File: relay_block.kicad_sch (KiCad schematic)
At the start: 49 parts, among them J4 Screw_Terminal_01x02, J5 Screw_Terminal_01x10, J6 Screw_Terminal_01x10, U10 TLP3558A, U11 TLP3558A, U12 TLP3558A, U13 TLP3558A, U14 TLP3558A, U15 TLP3558A, U16 TLP3558A, U17 TLP3558A, U18 TLP3558A, U19 TLP3558A, U20 TLP3558A, U21 TLP3558A, U22 TLP3558A, U23 TLP3558A, U24 TLP3558A, U25 TLP3558A, U4 TLP3558A, U5 TLP3558A, U6 TLP3558A, U7 TLP3558A, U8 TLP3558A, U9 TLP3558A

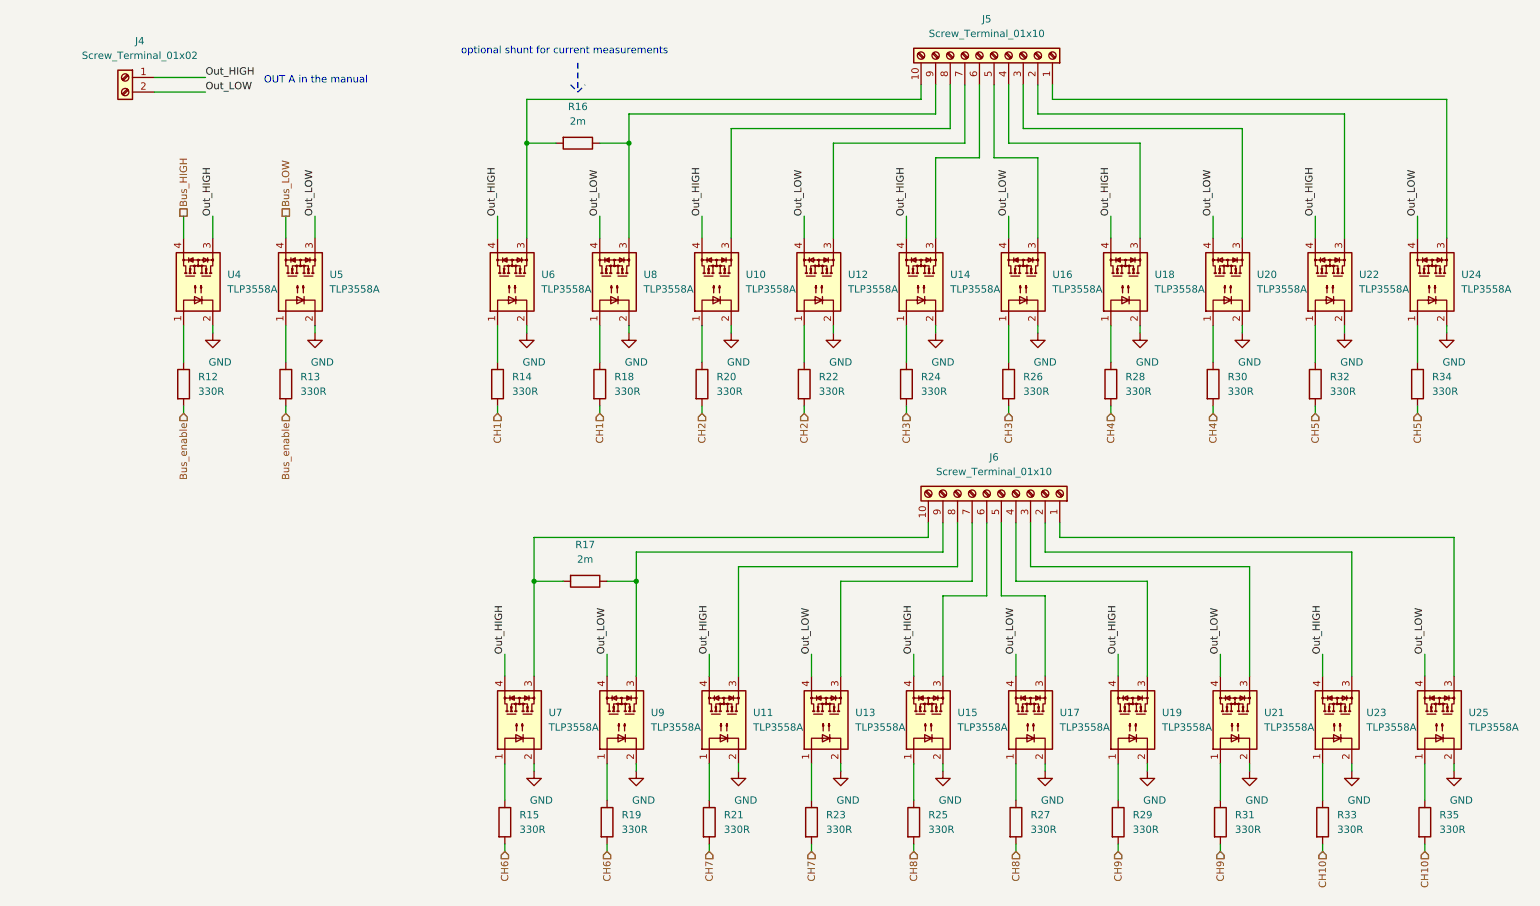
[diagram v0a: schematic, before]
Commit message: Replace the STM32 with an iCE40 FPGA (#3)
* Replaced the STM32 microcontroller with an iCE40 FPGA

* Bump version to 2.0.2, because of the update to KiCad 8

* Updated BOM properties

* Updated PCB image

* Updated readme for the FPGA version

* Updated links
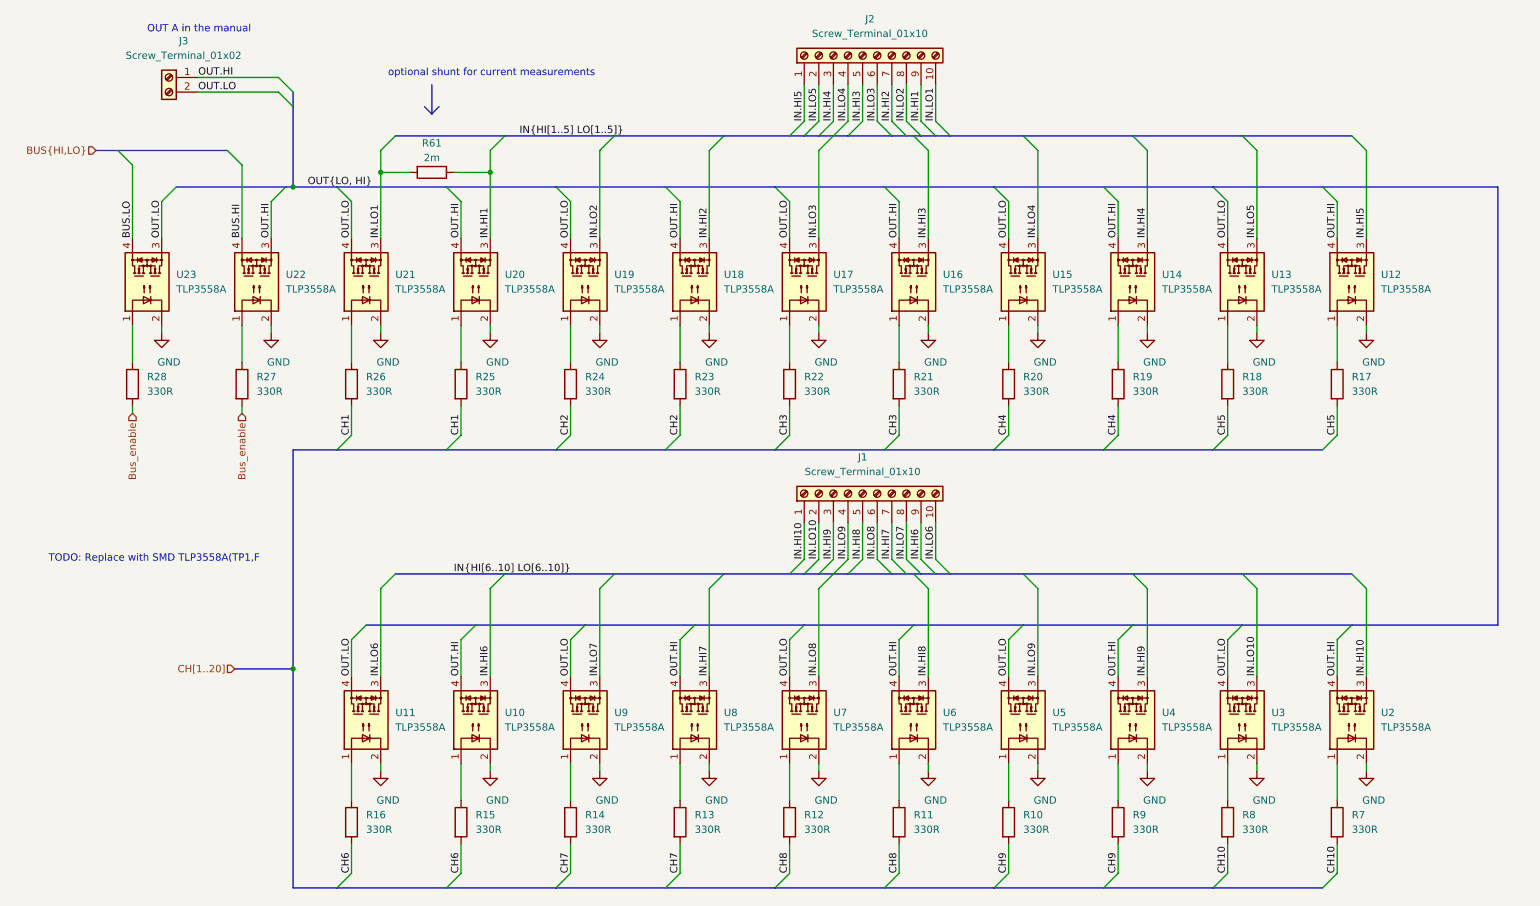
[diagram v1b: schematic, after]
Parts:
- removed R17: 2m, Resistor_SMD:R_2512_6332Metric, symbol Device:R
- J1: renamed from J6; RoHS By exemption -> Yes; Temperature Tstorage = –40 °C to 105 °C -> (none)
- J2: renamed from J5; RoHS By exemption -> Yes; Temperature Tstorage = –40 °C to 105 °C -> (none)
- J3: renamed from J4; RoHS By exemption -> Yes; Temperature Tstorage = –40 °C to 105 °C -> (none)
- R10: renamed from R29; Alternative (none) -> Yageo AC0603JR-07330RL or AC0603FR-07330RL; Note (none) -> 5% or better; PN CRCW0603330RJNEB -> CRCW0603330RJNEA
- R11: renamed from R27; Alternative (none) -> Yageo AC0603JR-07330RL or AC0603FR-07330RL; Note (none) -> 5% or better; PN CRCW0603330RJNEB -> CRCW0603330RJNEA
- R12: renamed from R25; Alternative (none) -> Yageo AC0603JR-07330RL or AC0603FR-07330RL; Note (none) -> 5% or better; PN CRCW0603330RJNEB -> CRCW0603330RJNEA
- R13: renamed from R23; Alternative (none) -> Yageo AC0603JR-07330RL or AC0603FR-07330RL; Note (none) -> 5% or better; PN CRCW0603330RJNEB -> CRCW0603330RJNEA
- R14: renamed from R21; Alternative (none) -> Yageo AC0603JR-07330RL or AC0603FR-07330RL; Note (none) -> 5% or better; PN CRCW0603330RJNEB -> CRCW0603330RJNEA
- R15: renamed from R19; Alternative (none) -> Yageo AC0603JR-07330RL or AC0603FR-07330RL; Note (none) -> 5% or better; PN CRCW0603330RJNEB -> CRCW0603330RJNEA
- R16: renamed from R15; Alternative (none) -> Yageo AC0603JR-07330RL or AC0603FR-07330RL; Note (none) -> 5% or better; PN CRCW0603330RJNEB -> CRCW0603330RJNEA
- R17: renamed from R34; Alternative (none) -> Yageo AC0603JR-07330RL or AC0603FR-07330RL; Note (none) -> 5% or better; PN CRCW0603330RJNEB -> CRCW0603330RJNEA
- R18: renamed from R32; Alternative (none) -> Yageo AC0603JR-07330RL or AC0603FR-07330RL; Note (none) -> 5% or better; PN CRCW0603330RJNEB -> CRCW0603330RJNEA
- R19: renamed from R30; Alternative (none) -> Yageo AC0603JR-07330RL or AC0603FR-07330RL; Note (none) -> 5% or better; PN CRCW0603330RJNEB -> CRCW0603330RJNEA
- R20: renamed from R28; Alternative (none) -> Yageo AC0603JR-07330RL or AC0603FR-07330RL; Note (none) -> 5% or better; PN CRCW0603330RJNEB -> CRCW0603330RJNEA
- R21: renamed from R26; Alternative (none) -> Yageo AC0603JR-07330RL or AC0603FR-07330RL; Note (none) -> 5% or better; PN CRCW0603330RJNEB -> CRCW0603330RJNEA
- R22: renamed from R24; Alternative (none) -> Yageo AC0603JR-07330RL or AC0603FR-07330RL; Note (none) -> 5% or better; PN CRCW0603330RJNEB -> CRCW0603330RJNEA
- R23: renamed from R22; Alternative (none) -> Yageo AC0603JR-07330RL or AC0603FR-07330RL; Note (none) -> 5% or better; PN CRCW0603330RJNEB -> CRCW0603330RJNEA
- R24: renamed from R20; Alternative (none) -> Yageo AC0603JR-07330RL or AC0603FR-07330RL; Note (none) -> 5% or better; PN CRCW0603330RJNEB -> CRCW0603330RJNEA
- R25: renamed from R18; Alternative (none) -> Yageo AC0603JR-07330RL or AC0603FR-07330RL; Note (none) -> 5% or better; PN CRCW0603330RJNEB -> CRCW0603330RJNEA
- R26: renamed from R14; Alternative (none) -> Yageo AC0603JR-07330RL or AC0603FR-07330RL; Note (none) -> 5% or better; PN CRCW0603330RJNEB -> CRCW0603330RJNEA
- R27: renamed from R12; Alternative (none) -> Yageo AC0603JR-07330RL or AC0603FR-07330RL; Note (none) -> 5% or better; PN CRCW0603330RJNEB -> CRCW0603330RJNEA
- R28: renamed from R13; Alternative (none) -> Yageo AC0603JR-07330RL or AC0603FR-07330RL; Note (none) -> 5% or better; PN CRCW0603330RJNEB -> CRCW0603330RJNEA
- R61: renamed from R16; Config (none) -> do not fit
- R7: renamed from R35; Alternative (none) -> Yageo AC0603JR-07330RL or AC0603FR-07330RL; Note (none) -> 5% or better; PN CRCW0603330RJNEB -> CRCW0603330RJNEA
- R8: renamed from R33; Alternative (none) -> Yageo AC0603JR-07330RL or AC0603FR-07330RL; Note (none) -> 5% or better; PN CRCW0603330RJNEB -> CRCW0603330RJNEA
- R9: renamed from R31; Alternative (none) -> Yageo AC0603JR-07330RL or AC0603FR-07330RL; Note (none) -> 5% or better; PN CRCW0603330RJNEB -> CRCW0603330RJNEA
- renumbered U9 to U10, U7 to U11, U24 to U12, U22 to U13, U20 to U14, U18 to U15, U14 to U17, U12 to U18, U10 to U19, U25 to U2, U8 to U20, U6 to U21, U4 to U22, U5 to U23, U23 to U3, U21 to U4, U19 to U5, U17 to U6, U15 to U7, U13 to U8, U11 to U9
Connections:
- net IN.LO1: now reaches J2.10 (Pin_10), R61.2, U21.3
- net IN.HI1: now reaches J2.9 (Pin_9), R61.1, U20.3
- net IN.HI5: now reaches J2.1 (Pin_1), U12.3
- net IN.LO5: now reaches J2.2 (Pin_2), U13.3
- net IN.HI4: now reaches J2.3 (Pin_3), U14.3
- net IN.LO4: now reaches J2.4 (Pin_4), U15.3
- net IN.HI3: now reaches J2.5 (Pin_5), U16.3
- net IN.LO3: now reaches J2.6 (Pin_6), U17.3
- net IN.HI2: now reaches J2.7 (Pin_7), U18.3
- net IN.LO2: now reaches J2.8 (Pin_8), U19.3
- net IN.LO6: now reaches J1.10 (Pin_10), U11.3
- net IN.HI10: now reaches J1.1 (Pin_1), U2.3
- net IN.LO10: now reaches J1.2 (Pin_2), U3.3
- net IN.HI9: now reaches J1.3 (Pin_3), U4.3
- net IN.LO9: now reaches J1.4 (Pin_4), U5.3
- net IN.HI8: now reaches J1.5 (Pin_5), U6.3
- net IN.LO8: now reaches J1.6 (Pin_6), U7.3
- net IN.HI7: now reaches J1.7 (Pin_7), U8.3
- net IN.LO7: now reaches J1.8 (Pin_8), U9.3
- net IN.HI6: now reaches J1.9 (Pin_9), U10.3
- net Bus_HIGH renamed BUS.HI
- net Bus_LOW renamed BUS.LO
- net Out_HIGH renamed OUT.LO
- net OUT.LO: now also J3.2 (Pin_2), U23.3; no longer J3.1 (Pin_1), U22.3
- net Out_LOW renamed OUT.HI
- net OUT.HI: now also J3.1 (Pin_1), U22.3; no longer J3.2 (Pin_2), U23.3
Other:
- note added: "TODO: Replace with SMD TLP3558A(TP1,F"
- moved on the sheet: J1, J2, J3, R10, R11, R12, R13, R14, R15, R16, R17, R18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
